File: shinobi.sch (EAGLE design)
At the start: 112 parts, among them J1 2171790001, J2 61300711121, J3 61301011121, J4 61300211121, J5 61300211121, U1 TV5725, U2 W9864G2JH-6, U3 ESP-06, U4 74ABT125PW, U5 Si5351A-B-GT, U6 CH340C, U7 TPS621351, U8 NCV8187AMN180TAG, Y1 27MHZ 10pF, Y2 25.0MHz 10pF

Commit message: update images, add eagle palette script
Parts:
- L2, L3, L4: value ? -> 10uH
- renumbered FB1 to L2, FB2 to L3, FB3 to L4
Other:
- note added: "CC BY-SA 4.0"

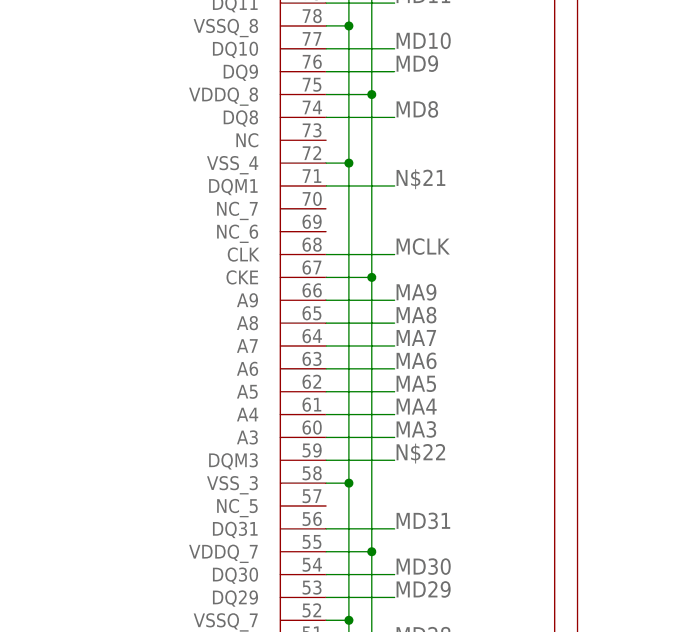
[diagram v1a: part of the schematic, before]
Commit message: fix gerber issue, update schematic.png
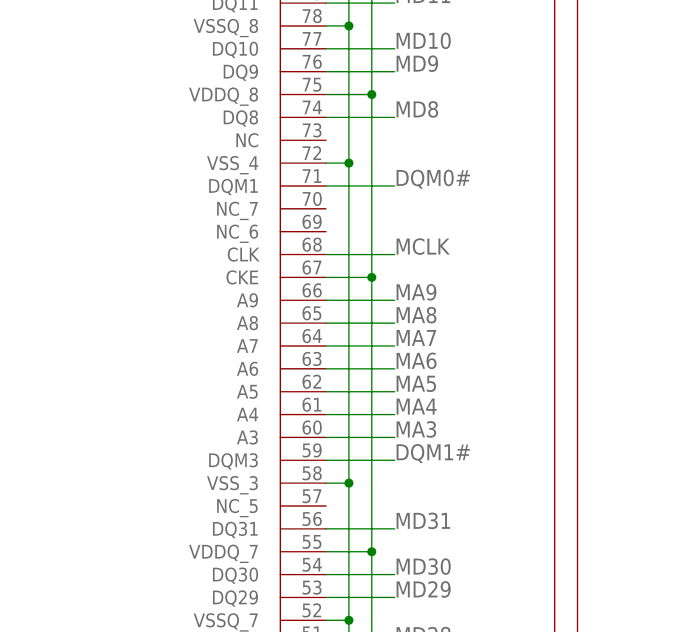
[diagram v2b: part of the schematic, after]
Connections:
- removed net N$21: U2.DQM1
- removed net N$22: U2.DQM3
- net DQM0#: now also U2.DQM1
- net DQM1#: now also U2.DQM3
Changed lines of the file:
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@@
 <pinref part="U2" gate="A" pin="DQM0"/>
+</segment>
+<segment>
+<wire x1="500.38" y1="142.24" x2="492.76" y2="142.24" width="0.1524" layer="91"/>
+<pinref part="U2" gate="A" pin="DQM1"/>
+<label x="500.38" y="142.24" size="1.778" layer="95"/>
 </segment>
 </net>
@@
 <label x="424.18" y="111.76" size="1.778" layer="95" rot="MR0"/>
 <pinref part="U2" gate="A" pin="DQM2"/>
+</segment>
+<segment>
+<wire x1="492.76" y1="111.76" x2="500.38" y2="111.76" width="0.1524" layer="91"/>
+<label x="500.38" y="111.76" size="1.778" layer="95"/>
+<pinref part="U2" gate="A" pin="DQM3"/>
 </segment>
 </net>
@@
 </segment>
 </net>
-<net name="N$21" class="0">
-<segment>
-<wire x1="492.76" y1="142.24" x2="500.38" y2="142.24" width="0.1524" layer="91"/>
-<label x="500.38" y="142.24" size="1.778" layer="95"/>
-<pinref part="U2" gate="A" pin="DQM1"/>
-</segment>
-</net>
-<net name="N$22" class="0">
-<segment>
-<wire x1="492.76" y1="111.76" x2="500.38" y2="111.76" width="0.1524" layer="91"/>
-<label x="500.38" y="111.76" size="1.778" layer="95"/>
-<pinref part="U2" gate="A" pin="DQM3"/>
-</segment>
-</net>

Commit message: update with correct ferrite beads
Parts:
- FB1, FB2, FB3: value 10uH -> 220Ω
- renumbered L2 to FB1, L3 to FB2, L4 to FB3
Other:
- note added: "x8"
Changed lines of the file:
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@@
 <?xml version="1.0" encoding="utf-8"?>
 <!DOCTYPE eagle SYSTEM "eagle.dtd">
-<eagle version="9.6.1">
+<eagle version="9.6.2">
 <drawing>
 <settings>
@@
 <part name="GND38" library="SparkFun-PowerSymbols" deviceset="GND" device=""/>
 <part name="GND39" library="SparkFun-PowerSymbols" deviceset="GND" device=""/>
-<part name="L2" library="resistor" library_urn="urn:adsk.eagle:library:2745533" deviceset="L0402" device="" package3d_urn="urn:adsk.eagle:package:2745538/3" value="10uH"/>
-<part name="L3" library="resistor" library_urn="urn:adsk.eagle:library:2745533" deviceset="L0402" device="" package3d_urn="urn:adsk.eagle:package:2745538/3" value="10uH"/>
-<part name="L4" library="resistor" library_urn="urn:adsk.eagle:library:2745533" deviceset="L0402" device="" package3d_urn="urn:adsk.eagle:package:2745538/3" value="10uH"/>
+<part name="FB1" library="resistor" library_urn="urn:adsk.eagle:library:2745533" deviceset="L0402" device="" package3d_urn="urn:adsk.eagle:package:2745538/3" value="220Ω"/>
+<part name="FB2" library="resistor" library_urn="urn:adsk.eagle:library:2745533" deviceset="L0402" device="" package3d_urn="urn:adsk.eagle:package:2745538/3" value="220Ω"/>
+<part name="FB3" library="resistor" library_urn="urn:adsk.eagle:library:2745533" deviceset="L0402" device="" package3d_urn="urn:adsk.eagle:package:2745538/3" value="220Ω"/>
 <part name="C56" library="resistor" library_urn="urn:adsk.eagle:library:2745533" deviceset="C-US" device="C0402" package3d_urn="urn:adsk.eagle:package:2745540/2" value="15pF"/>
 <part name="C57" library="resistor" library_urn="urn:adsk.eagle:library:2745533" deviceset="C-US" device="C0402" package3d_urn="urn:adsk.eagle:package:2745540/2" value="15pF"/>
@@
 <rectangle x1="484.4923" y1="32.9057" x2="484.5685" y2="32.9311" layer="200"/>
 <text x="480.441" y="8.7122" size="2.54" layer="97" font="vector">CC BY-SA 4.0</text>
+<text x="474.98" y="46.736" size="1.778" layer="95">x8</text>
 </plain>
 <instances>
@@
 <instance part="C43" gate="G$1" x="441.96" y="55.88" smashed="yes">
 <attribute name="NAME" x="442.976" y="56.515" size="1.778" layer="95"/>
-<attribute name="VALUE" x="442.976" y="51.689" size="1.778" layer="96"/>
 </instance>
 <instance part="C44" gate="G$1" x="447.04" y="55.88" smashed="yes">
 <attribute name="NAME" x="448.056" y="56.515" size="1.778" layer="95"/>
-<attribute name="VALUE" x="448.056" y="51.689" size="1.778" layer="96"/>
 </instance>
 <instance part="C45" gate="G$1" x="452.12" y="55.88" smashed="yes">
 <attribute name="NAME" x="453.136" y="56.515" size="1.778" layer="95"/>
-<attribute name="VALUE" x="453.136" y="51.689" size="1.778" layer="96"/>
 </instance>
 <instance part="C46" gate="G$1" x="457.2" y="55.88" smashed="yes">
 <attribute name="NAME" x="458.216" y="56.515" size="1.778" layer="95"/>
-<attribute name="VALUE" x="458.216" y="51.689" size="1.778" layer="96"/>
 </instance>
 <instance part="C47" gate="G$1" x="462.28" y="55.88" smashed="yes">
 <attribute name="NAME" x="463.296" y="56.515" size="1.778" layer="95"/>
-<attribute name="VALUE" x="463.296" y="51.689" size="1.778" layer="96"/>
 </instance>
 <instance part="C48" gate="G$1" x="467.36" y="55.88" smashed="yes">
 <attribute name="NAME" x="468.376" y="56.515" size="1.778" layer="95"/>
-<attribute name="VALUE" x="468.376" y="51.689" size="1.778" layer="96"/>
 </instance>
 <instance part="C49" gate="G$1" x="472.44" y="55.88" smashed="yes">
 <attribute name="NAME" x="473.456" y="56.515" size="1.778" layer="95"/>
-<attribute name="VALUE" x="473.456" y="51.689" size="1.778" layer="96"/>
 </instance>
 <instance part="C50" gate="G$1" x="477.52" y="55.88" smashed="yes">
 <attribute name="NAME" x="478.536" y="56.515" size="1.778" layer="95"/>
-<attribute name="VALUE" x="478.536" y="51.689" size="1.778" layer="96"/>
+<attribute name="VALUE" x="468.122" y="46.736" size="1.778" layer="96"/>
 </instance>
 <instance part="+3V16" gate="G$1" x="462.28" y="63.5" smashed="yes">
@@
 <attribute name="VALUE" x="76.2" y="187.96" size="1.778" layer="96" font="vector" rot="MR0"/>
 </instance>
-<instance part="L2" gate="G$1" x="114.3" y="218.44" smashed="yes" rot="MR0">
+<instance part="FB1" gate="G$1" x="114.3" y="218.44" smashed="yes" rot="MR0">
 <attribute name="NAME" x="111.252" y="219.71" size="1.778" layer="95" rot="MR0"/>
 <attribute name="VALUE" x="118.618" y="219.71" size="1.778" layer="96" rot="MR0"/>
 </instance>
-<instance part="L3" gate="G$1" x="114.3" y="205.74" smashed="yes" rot="MR0">
+<instance part="FB2" gate="G$1" x="114.3" y="205.74" smashed="yes" rot="MR0">
 <attribute name="NAME" x="111.252" y="207.264" size="1.778" layer="95" rot="MR0"/>
 <attribute name="VALUE" x="118.364" y="207.264" size="1.778" layer="96" rot="MR0"/>
 </instance>
-<instance part="L4" gate="G$1" x="114.3" y="193.04" smashed="yes" rot="MR0">
+<instance part="FB3" gate="G$1" x="114.3" y="193.04" smashed="yes" rot="MR0">
 <attribute name="NAME" x="110.998" y="194.31" size="1.778" layer="95" rot="MR0"/>
 <attribute name="VALUE" x="117.856" y="194.31" size="1.778" layer="96" rot="MR0"/>
@@
 <segment>
 <pinref part="C56" gate="G$1" pin="2"/>
-<pinref part="L2" gate="G$1" pin="P$2"/>
+<pinref part="FB1" gate="G$1" pin="P$2"/>
 <wire x1="110.49" y1="215.138" x2="109.22" y2="215.138" width="0.1524" layer="91"/>
 <wire x1="109.22" y1="215.138" x2="109.22" y2="218.44" width="0.1524" layer="91"/>
@@
 <segment>
 <pinref part="C57" gate="G$1" pin="2"/>
-<pinref part="L3" gate="G$1" pin="P$2"/>
+<pinref part="FB2" gate="G$1" pin="P$2"/>
 <wire x1="110.49" y1="202.438" x2="109.22" y2="202.438" width="0.1524" layer="91"/>
 <wire x1="109.22" y1="202.438" x2="109.22" y2="205.74" width="0.1524" layer="91"/>
@@
 <segment>
 <pinref part="C58" gate="G$1" pin="2"/>
-<pinref part="L4" gate="G$1" pin="P$2"/>
+<pinref part="FB3" gate="G$1" pin="P$2"/>
 <wire x1="110.49" y1="189.738" x2="109.22" y2="189.738" width="0.1524" layer="91"/>
 <wire x1="109.22" y1="189.738" x2="109.22" y2="193.04" width="0.1524" layer="91"/>
@@
 <segment>
 <pinref part="C58" gate="G$1" pin="1"/>
-<pinref part="L4" gate="G$1" pin="P$1"/>
+<pinref part="FB3" gate="G$1" pin="P$1"/>
 <wire x1="118.11" y1="189.738" x2="119.38" y2="189.738" width="0.1524" layer="91"/>
 <wire x1="119.38" y1="189.738" x2="119.38" y2="193.04" width="0.1524" layer="91"/>
@@
 <segment>
 <pinref part="C57" gate="G$1" pin="1"/>
-<pinref part="L3" gate="G$1" pin="P$1"/>
+<pinref part="FB2" gate="G$1" pin="P$1"/>
 <wire x1="118.11" y1="202.438" x2="119.38" y2="202.438" width="0.1524" layer="91"/>
 <wire x1="119.38" y1="202.438" x2="119.38" y2="205.74" width="0.1524" layer="91"/>
@@
 <segment>
 <pinref part="C56" gate="G$1" pin="1"/>
-<pinref part="L2" gate="G$1" pin="P$1"/>
+<pinref part="FB1" gate="G$1" pin="P$1"/>
 <wire x1="118.11" y1="215.138" x2="119.38" y2="215.138" width="0.1524" layer="91"/>
 <wire x1="119.38" y1="215.138" x2="119.38" y2="218.44" width="0.1524" layer="91"/>
